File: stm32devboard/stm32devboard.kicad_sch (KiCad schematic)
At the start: 44 parts, among them J1 Conn_01x20, J2 Conn_01x20, J3 USB_C_Receptacle_USB2.0, J4 ARM_SWD_TagConnect_TC2030-NL, SW1 SW_SPST, SW2 SW_SPST, U1 STM32F042C6Tx, U2 AP63203WU, U3 TCAN332, U4 IP4234CZ6,125, X1 ECS-160-10-36Q-ES-TR

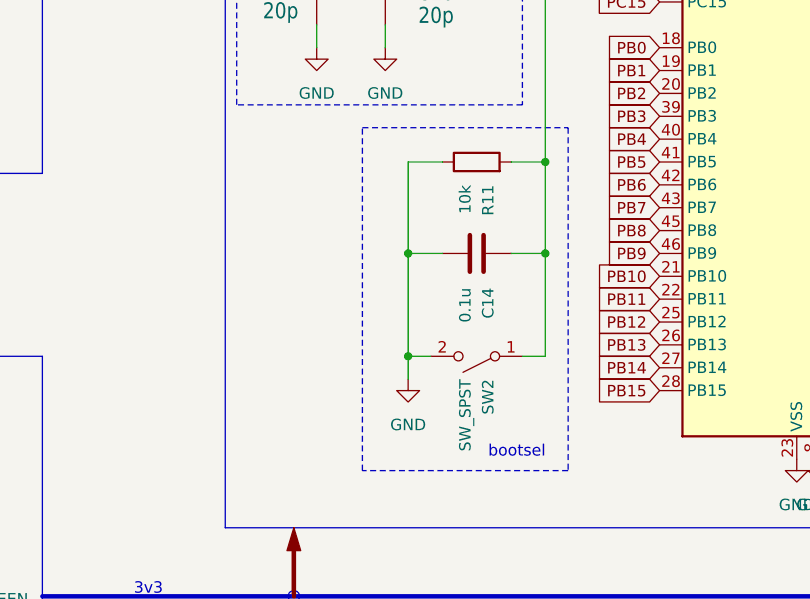
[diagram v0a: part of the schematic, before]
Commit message: Fixed boot button and updated silkscreen
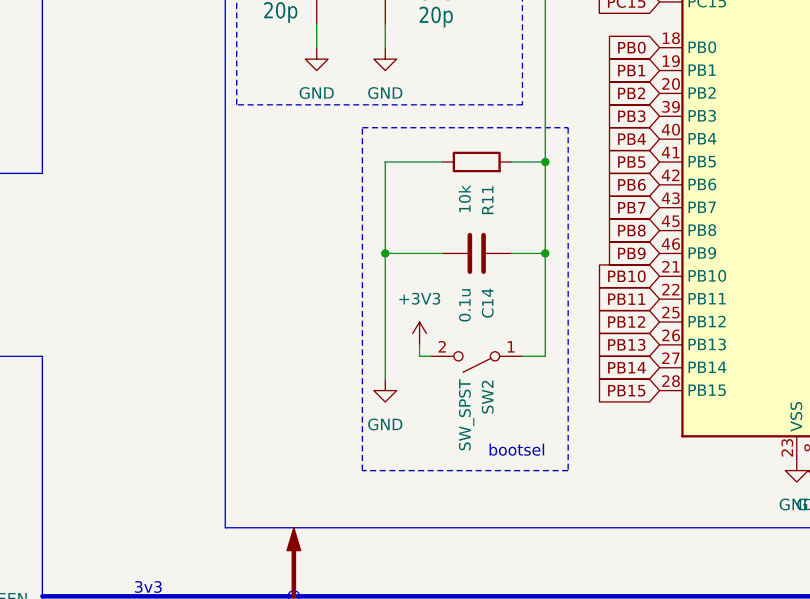
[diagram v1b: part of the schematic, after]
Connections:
- net +3V3: now also SW2.2 (B)
- net GND: no longer SW2.2 (B)
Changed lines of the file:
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@@
 	(title_block
 		(title "minTS Microcontroller Devboad")
-		(date "2024-02-25")
-		(rev "V1.1")
+		(date "2024-05-02")
+		(rev "V1.2")
 		(company "PSAS")
 		(comment 1 "Benjamin Crall")
@@
 	)
 	(junction
-		(at 154.94 138.43)
-		(diameter 0)
-		(color 0 0 0 0)
-	)
-	(junction
 		(at 142.24 83.82)
 		(diameter 0)
@@
 	)
 	(junction
-		(at 154.94 149.86)
+		(at 81.28 180.34)
 		(diameter 0)
 		(color 0 0 0 0)
 	)
 	(junction
-		(at 81.28 180.34)
+		(at 33.02 172.72)
 		(diameter 0)
 		(color 0 0 0 0)
 	)
 	(junction
-		(at 33.02 172.72)
+		(at 152.4 138.43)
 		(diameter 0)
 		(color 0 0 0 0)
@@
 	(wire
 		(pts
-			(xy 154.94 128.27) (xy 154.94 138.43)
+			(xy 152.4 128.27) (xy 152.4 138.43)
 		)
 		(stroke
@@
 	(wire
 		(pts
+			(xy 156.21 148.59) (xy 156.21 149.86)
+		)
+		(stroke
+			(width 0)
+			(type default)
+		)
+	)
+	(wire
+		(pts
 			(xy 351.79 151.13) (xy 351.79 153.67)
 		)
@@
 	(wire
 		(pts
-			(xy 154.94 152.4) (xy 154.94 149.86)
-		)
-		(stroke
-			(width 0)
-			(type default)
-		)
-	)
-	(wire
-		(pts
 			(xy 63.5 67.31) (xy 78.74 67.31)
 		)
@@
 	(wire
 		(pts
-			(xy 154.94 138.43) (xy 154.94 149.86)
+			(xy 152.4 138.43) (xy 152.4 152.4)
 		)
 		(stroke
@@
 	(wire
 		(pts
-			(xy 154.94 149.86) (xy 157.48 149.86)
-		)
-		(stroke
-			(width 0)
-			(type default)
-		)
-	)
-	(wire
-		(pts
 			(xy 195.58 85.09) (xy 195.58 80.01)
 		)
@@
 	(wire
 		(pts
-			(xy 158.75 128.27) (xy 154.94 128.27)
+			(xy 158.75 128.27) (xy 152.4 128.27)
 		)
 		(stroke
@@
 	(wire
 		(pts
+			(xy 157.48 149.86) (xy 156.21 149.86)
+		)
+		(stroke
+			(width 0)
+			(type default)
+		)
+	)
+	(wire
+		(pts
 			(xy 238.76 90.17) (xy 238.76 92.71)
 		)
@@
 	(wire
 		(pts
-			(xy 198.12 80.01) (xy 203.2 80.01)
+			(xy 152.4 138.43) (xy 158.75 138.43)
 		)
 		(stroke
@@
 	(wire
 		(pts
-			(xy 154.94 138.43) (xy 158.75 138.43)
+			(xy 198.12 80.01) (xy 203.2 80.01)
 		)
 		(stroke
@@
 	(symbol
 		(lib_id "power:GND")
-		(at 154.94 152.4 0)
+		(at 152.4 152.4 0)
 		(unit 1)
 		(exclude_from_sim no)
@@
 		(fields_autoplaced yes)
 		(property "Reference" "#PWR040"
-			(at 154.94 158.75 0)
+			(at 152.4 158.75 0)
 			(effects
 				(font
@@
 		)
 		(property "Value" "GND"
-			(at 154.94 157.48 0)
+			(at 152.4 157.48 0)
 			(effects
 				(font
@@
 		)
 		(property "Footprint" ""
-			(at 154.94 152.4 0)
+			(at 152.4 152.4 0)
 			(effects
 				(font
@@
 		)
 		(property "Datasheet" ""
-			(at 154.94 152.4 0)
+			(at 152.4 152.4 0)
 			(effects
 				(font
@@
 		)
 		(property "Description" ""
-			(at 154.94 152.4 0)
+			(at 152.4 152.4 0)
 			(effects
 				(font
@@
 					(unit 1)
 				)
+			)
+		)
+	)
+	(symbol
+		(lib_name "+3V3_1")
+		(lib_id "power:+3V3")
+		(at 156.21 148.59 0)
+		(unit 1)
+		(exclude_from_sim no)
+		(in_bom yes)
+		(on_board yes)
+		(dnp no)
+		(fields_autoplaced yes)
+		(property "Reference" "#PWR046"
+			(at 156.21 152.4 0)
+			(effects
+				(font
+					(size 1.27 1.27)
+				)
+				(hide yes)
+			)
+		)
+		(property "Value" "+3V3"
+			(at 156.21 143.51 0)
+			(effects
+				(font
+					(size 1.27 1.27)
+				)
+			)
+		)
+		(property "Footprint" ""
+			(at 156.21 148.59 0)
+			(effects
+				(font
+					(size 1.27 1.27)
+				)
+				(hide yes)
+			)
+		)
+		(property "Datasheet" ""
+			(at 156.21 148.59 0)
+			(effects
+				(font
+					(size 1.27 1.27)
+				)
+				(hide yes)
+			)
+		)
+		(property "Description" "Power symbol creates a global label with name \"+3V3\""
+			(at 156.21 148.59 0)
+			(effects
+				(font
+					(size 1.27 1.27)
+				)
+				(hide yes)
+			)
+		)
+		(pin "1"
+		)
+		(instances
+			(project "stm32devboard"
+				(path "/96be6751-0ff1-459c-b196-8024d4959d86"
+					(reference "#PWR046")
+					(unit 1)
+				)

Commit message: Prep for assembally
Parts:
- J3: DPN USB4105-GF-A -> 664-12402012E212ACT-ND; MPN 2073-USB4105-GF-ACT-ND -> 12402012E212A
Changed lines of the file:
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@@
 			)
 		)
-		(property "DPN" "USB4105-GF-A"
+		(property "DPN" "664-12402012E212ACT-ND"
 			(at 48.26 82.55 0)
 			(effects
@@
 			)
 		)
-		(property "MPN" "2073-USB4105-GF-ACT-ND"
+		(property "MPN" "12402012E212A"
 			(at 48.26 82.55 0)
 			(effects

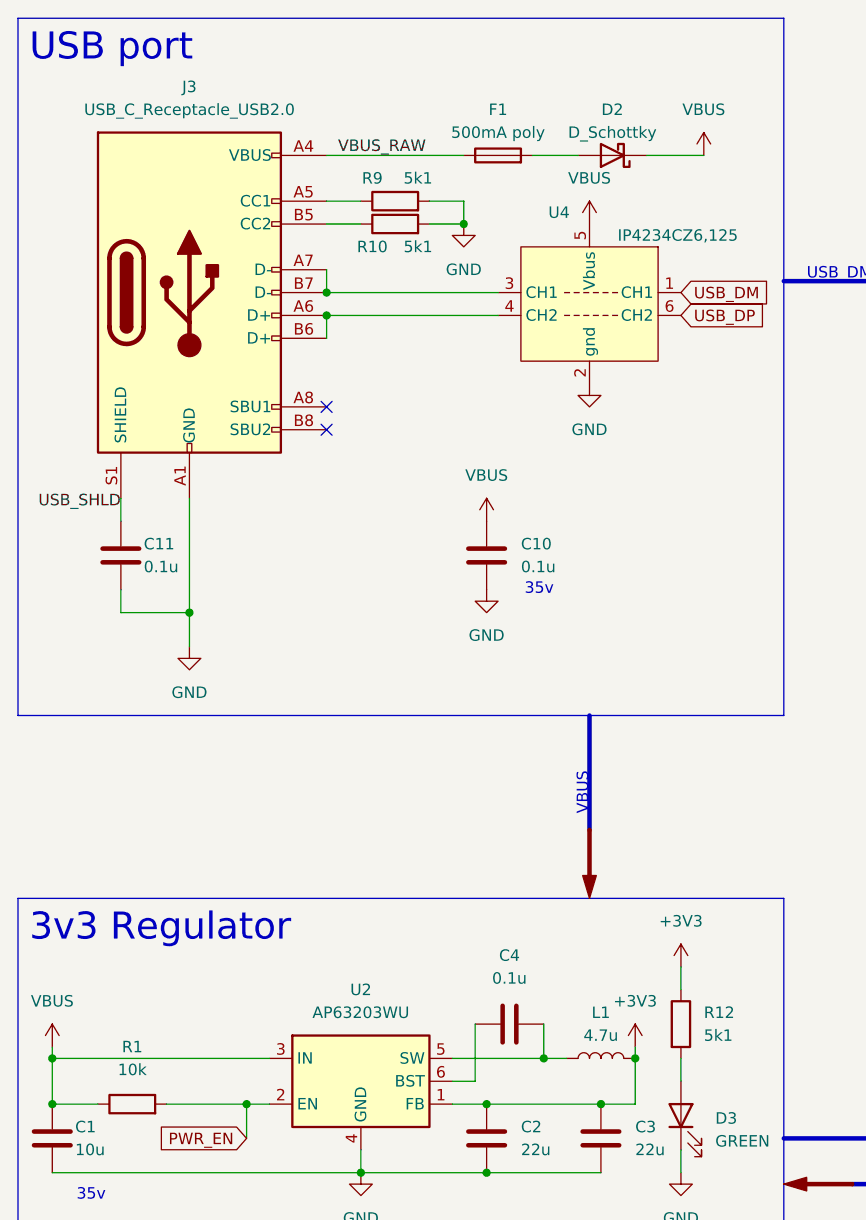
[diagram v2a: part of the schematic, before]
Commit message: Fix for TVS diode to be set to <=5V
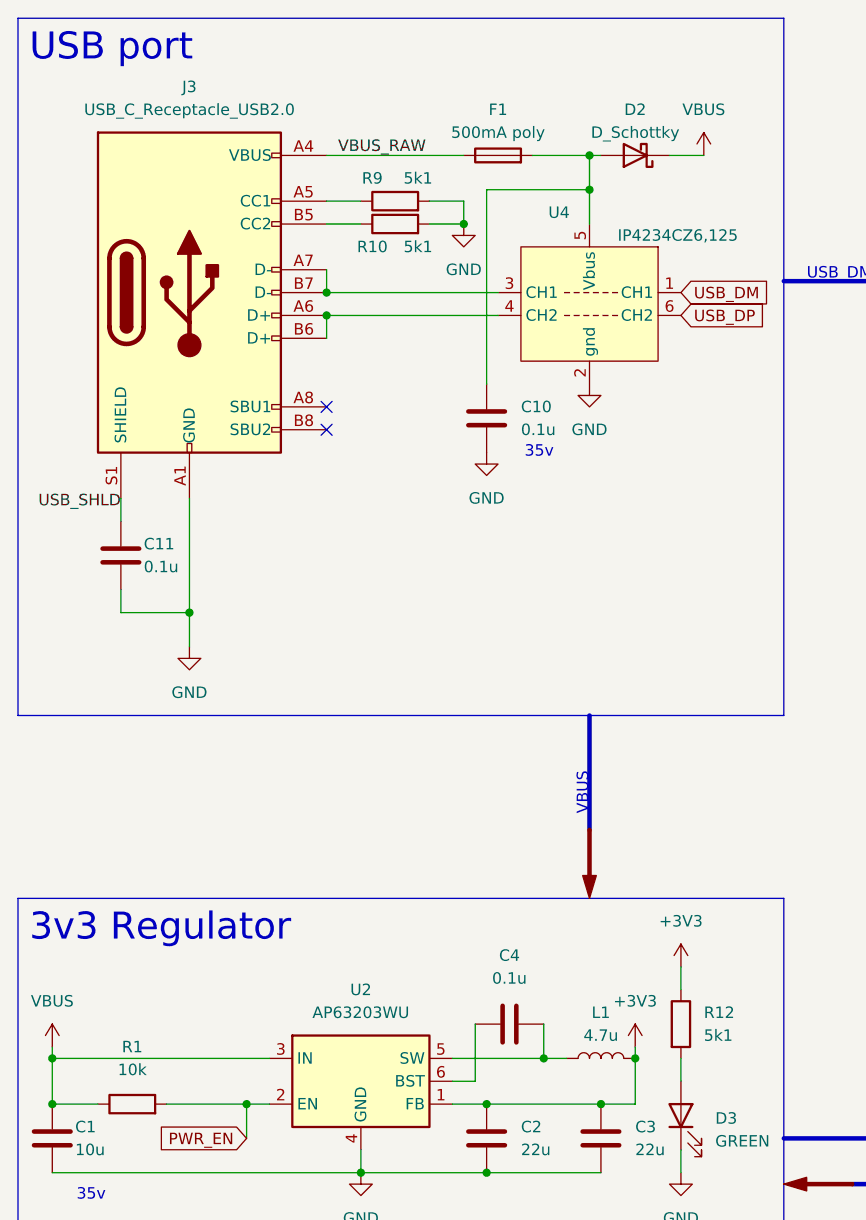
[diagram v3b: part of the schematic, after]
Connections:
- net VBUS: no longer C10.1, U4.5 (Vbus)
- net at D2.2 (A), F1.2: now also C10.1, U4.5 (Vbus)
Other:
- moved on the sheet: C10, D2

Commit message: Updated schematic and board to fab run of v1.3 on 2026-01-27.
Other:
- company: PSAS -> Portland State Aerospace Society
- title: minTS Microcontroller Devboad -> minTS STM32 Microcontroller Board
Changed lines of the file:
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@@
 	(paper "USLedger")
 	(title_block
-		(title "minTS Microcontroller Devboad")
-		(date "2024-05-02")
-		(rev "V1.2")
-		(company "PSAS")
-		(comment 1 "Benjamin Crall")
+		(title "minTS STM32 Microcontroller Board")
+		(date "2026-01-27")
+		(rev "V1.3")
+		(company "Portland State Aerospace Society")
 	)
 	(circle
